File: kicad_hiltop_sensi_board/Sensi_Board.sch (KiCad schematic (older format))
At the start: 146 parts, among them J1 Conn_02x06_Counter_Clockwise, J10 Conn_ARM_JTAG_SWD_10, J2 Conn_02x06_Counter_Clockwise, J3 Conn_03x32_DIN41612, J4 Conn_02x06_Counter_Clockwise, J5 Conn_02x06_Counter_Clockwise, J6 Conn_02x06_Counter_Clockwise, J7 Conn_02x06_Counter_Clockwise, J8 Conn_02x06_Counter_Clockwise, U1 INA250A4, U2 LD1117S33TR_SOT223, U3 AT25DN512CSSHF-B, U6 LM75B

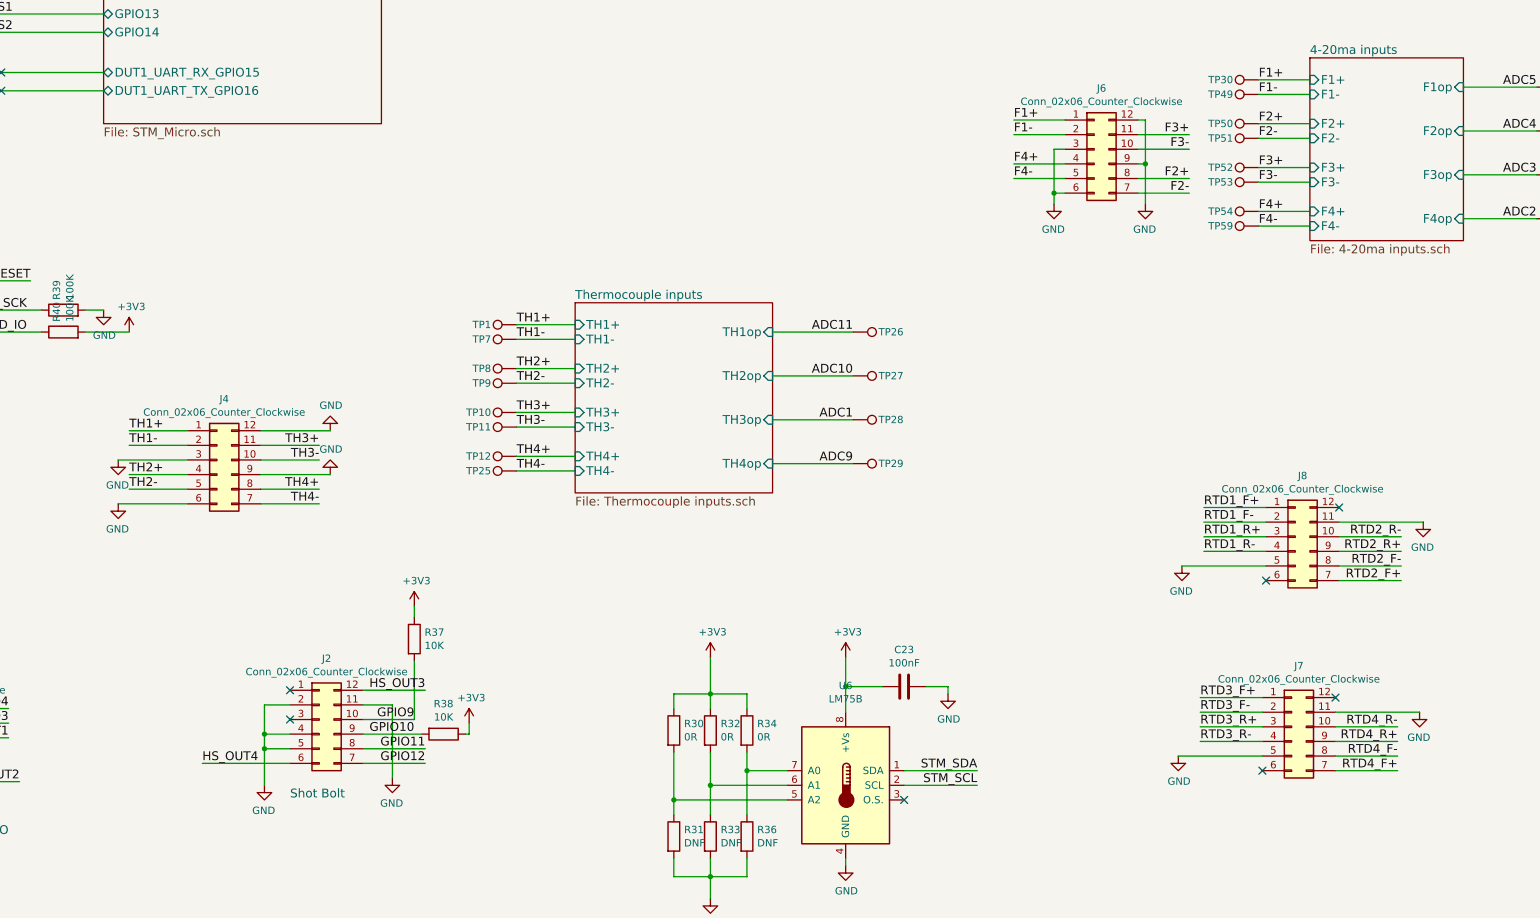
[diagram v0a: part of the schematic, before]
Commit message: Most of the routing of the sensi board complete
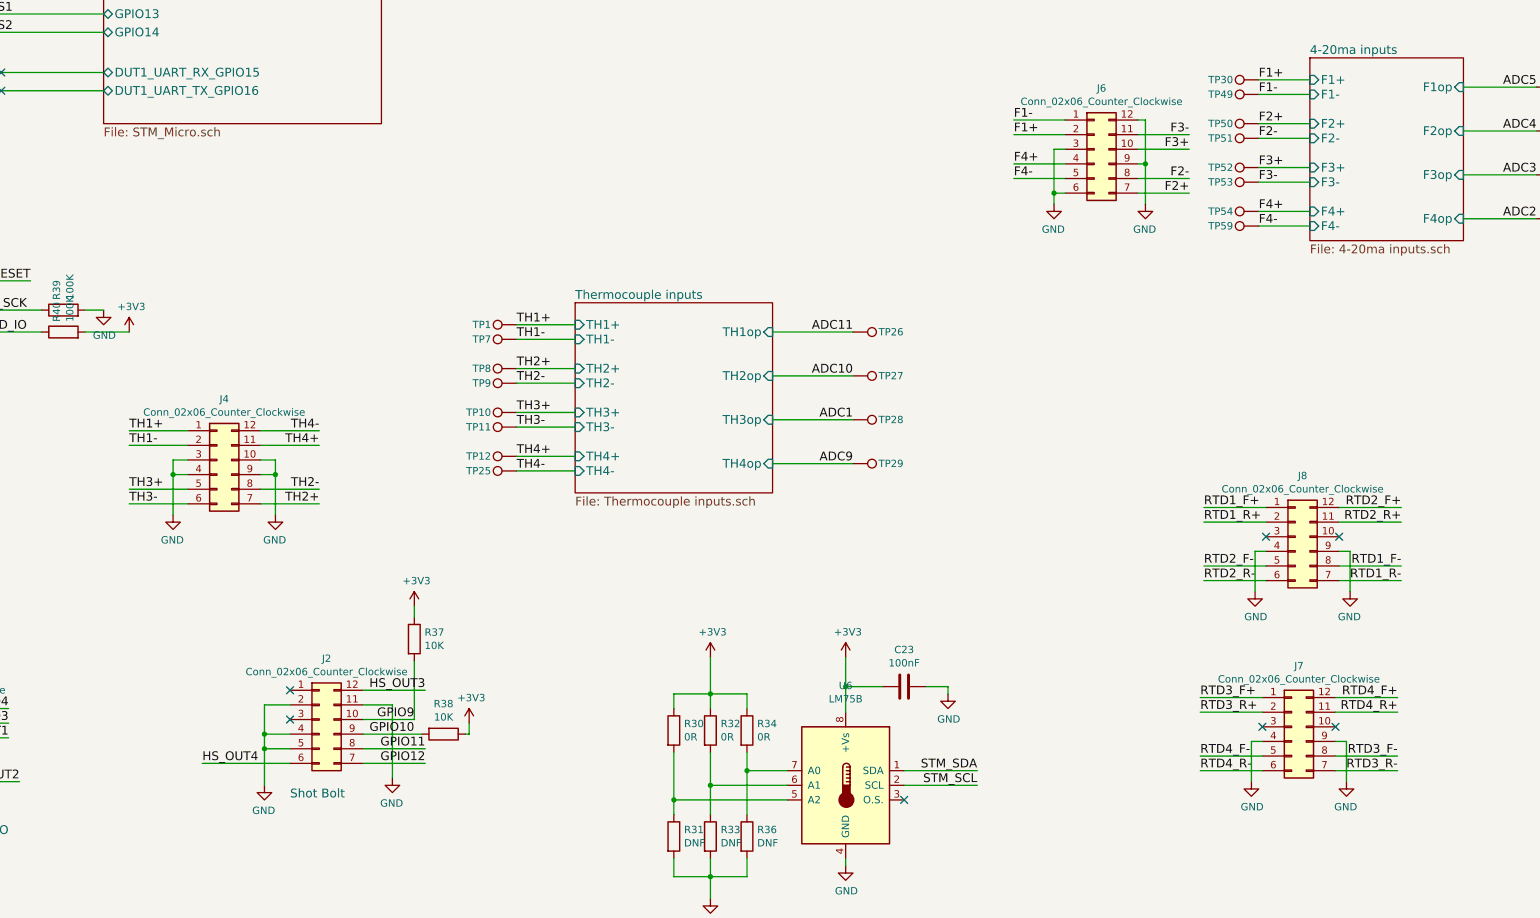
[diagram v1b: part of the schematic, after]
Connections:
- wire segments 522 -> 530
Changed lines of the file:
@@
 RTD3_R-
 Wire Wire Line
-	11150 11150 10725 11150
-Wire Wire Line
-	10725 11050 11150 11050
-Wire Wire Line
-	11150 11250 10725 11250
-Text Label 10725 11050 0    60   ~ 0
-RTD3_F+
-Text Label 10725 11150 0    60   ~ 0
-RTD3_F-
-Text Label 10725 11250 0    60   ~ 0
-RTD3_R+
-Text Label 10725 11350 0    60   ~ 0
-RTD3_R-
+	11650 11050 12075 11050
 Wire Wire Line
 	14475 12075 14050 12075
@@
 	14475 11550 14050 11550
 Wire Wire Line
-	11150 11350 10725 11350
+	11650 11150 12075 11150
 Text Label 6050 8500 0    60   ~ 0
 TH1+
@@
 TH1-
 Wire Wire Line
-	3800 9525 3400 9525
+	4300 9225 4700 9225
+Wire Wire Line
+	4300 9325 4700 9325
+Text Label 4700 9725 2    60   ~ 0
+TH2+
+Text Label 4700 9625 2    60   ~ 0
+TH2-
 Wire Wire Line
 	3800 9625 3400 9625
-Text Label 3400 9525 0    60   ~ 0
-TH2+
+Wire Wire Line
+	3800 9725 3400 9725
 Text Label 3400 9625 0    60   ~ 0
-TH2-
-Wire Wire Line
-	4300 9325 4700 9325
-Wire Wire Line
-	4300 9425 4700 9425
+TH3+
+Text Label 3400 9725 0    60   ~ 0
+TH3-
+Wire Wire Line
+	4300 9625 4700 9625
+Wire Wire Line
+	4300 9725 4700 9725
 Text Label 4700 9325 2    60   ~ 0
-TH3+
-Text Label 4700 9425 2    60   ~ 0
-TH3-
-Wire Wire Line
-	4300 9625 4700 9625
-Wire Wire Line
-	4300 9725 4700 9725
-Text Label 4700 9625 2    60   ~ 0
 TH4+
-Text Label 4700 9725 2    60   ~ 0
+Text Label 4700 9225 2    60   ~ 0
 TH4-
 Wire Wire Line
@@
 L power:GND #PWR0106
 U 1 1 5E8A9D77
-P 3325 9425
-F 0 "#PWR0106" H 3325 9175 50  0001 C CNN
-F 1 "GND" H 3330 9252 50  0000 C CNN
-F 2 "" H 3325 9425 50  0001 C CNN
-F 3 "" H 3325 9425 50  0001 C CNN
-	1    3325 9425
+P 3700 9800
+F 0 "#PWR0106" H 3700 9550 50  0001 C CNN
+F 1 "GND" H 3705 9627 50  0000 C CNN
+F 2 "" H 3700 9800 50  0001 C CNN
+F 3 "" H 3700 9800 50  0001 C CNN
+	1    3700 9800
 	-1   0    0    -1
 $EndComp
-Wire Wire Line
-	3800 9425 3325 9425
 $Comp
 L power:GND #PWR0107
 U 1 1 5E9010FA
-P 3325 9725
-F 0 "#PWR0107" H 3325 9475 50  0001 C CNN
-F 1 "GND" H 3330 9552 50  0000 C CNN
-F 2 "" H 3325 9725 50  0001 C CNN
-F 3 "" H 3325 9725 50  0001 C CNN
-	1    3325 9725
+P 4400 9800
+F 0 "#PWR0107" H 4400 9550 50  0001 C CNN
+F 1 "GND" H 4405 9627 50  0000 C CNN
+F 2 "" H 4400 9800 50  0001 C CNN
+F 3 "" H 4400 9800 50  0001 C CNN
+	1    4400 9800
 	-1   0    0    -1
 $EndComp
-Wire Wire Line
-	3800 9725 3325 9725
-$Comp
-L power:GND #PWR0108
-U 1 1 5E9587C9
-P 4775 9525
-F 0 "#PWR0108" H 4775 9275 50  0001 C CNN
-F 1 "GND" H 4780 9352 50  0000 C CNN
-F 2 "" H 4775 9525 50  0001 C CNN
-F 3 "" H 4775 9525 50  0001 C CNN
-	1    4775 9525
-	1    0    0    1
-$EndComp
-Wire Wire Line
-	4300 9525 4775 9525
-$Comp
-L power:GND #PWR0198
-U 1 1 5E9B0679
-P 4775 9225
-F 0 "#PWR0198" H 4775 8975 50  0001 C CNN
-F 1 "GND" H 4780 9052 50  0000 C CNN
-F 2 "" H 4775 9225 50  0001 C CNN
-F 3 "" H 4775 9225 50  0001 C CNN
-	1    4775 9225
-	1    0    0    1
-$EndComp
-Wire Wire Line
-	4300 9225 4775 9225
 Text Label 2575 11325 2    60   ~ 0
 HS_OUT1
@@
 Wire Wire Line
 	9800 7200 9450 7200
+Text Label 9450 7100 0    60   ~ 0
+F1-
 Text Label 9450 7200 0    60   ~ 0
-F1-
-Text Label 9450 7100 0    60   ~ 0
 F1+
 Wire Wire Line
@@
 Wire Wire Line
 	10300 7300 10650 7300
+Text Label 10650 7300 2    60   ~ 0
+F3+
 Text Label 10650 7200 2    60   ~ 0
-F3+
-Text Label 10650 7300 2    60   ~ 0
 F3-
 Wire Wire Line
@@
 $EndComp
 Wire Wire Line
+	11675 10150 12100 10150
+Wire Wire Line
+	10750 9750 11175 9750
+Wire Wire Line
 	11175 9850 10750 9850
 Wire Wire Line
-	10750 9750 11175 9750
-Wire Wire Line
-	11175 9950 10750 9950
-Wire Wire Line
-	11175 10050 10750 10050
+	11675 10250 12100 10250
 Text Label 10750 9750 0    60   ~ 0
 RTD1_F+
+Text Label 12100 10150 2    60   ~ 0
+RTD1_F-
 Text Label 10750 9850 0    60   ~ 0
-RTD1_F-
-Text Label 10750 9950 0    60   ~ 0
 RTD1_R+
-Text Label 10750 10050 0    60   ~ 0
+Text Label 12100 10250 2    60   ~ 0
 RTD1_R-
 Wire Wire Line
-	11175 10150 10600 10150
-$Comp
-L power:GND #PWR0258
-U 1 1 5D917155
-P 10600 10150
-F 0 "#PWR0258" H 10600 9900 50  0001 C CNN
-F 1 "GND" H 10605 9977 50  0000 C CNN
-F 2 "" H 10600 10150 50  0001 C CNN
-F 3 "" H 10600 10150 50  0001 C CNN
-	1    10600 10150
-	-1   0    0    -1
-$EndComp
-Wire Wire Line
-	11675 10150 12100 10150
-Wire Wire Line
-	12100 10250 11675 10250
-Wire Wire Line
-	11675 10050 12100 10050
-Wire Wire Line
-	11675 9950 12100 9950
-Text Label 12100 10250 2    60   ~ 0
+	11175 10150 10750 10150
+Wire Wire Line
+	12100 9750 11675 9750
+Wire Wire Line
+	11675 9850 12100 9850
+Wire Wire Line
+	11175 10250 10750 10250
+Text Label 12100 9750 2    60   ~ 0
 RTD2_F+
-Text Label 12100 10150 2    60   ~ 0
+Text Label 10750 10150 0    60   ~ 0
 RTD2_F-
-Text Label 12100 10050 2    60   ~ 0
+Text Label 12100 9850 2    60   ~ 0
 RTD2_R+
-Text Label 12100 9950 2    60   ~ 0
-RTD2_R-
-$Comp
-L power:GND #PWR0261
-U 1 1 5D9F6FB6
-P 12250 9850
-F 0 "#PWR0261" H 12250 9600 50  0001 C CNN
-F 1 "GND" H 12255 9677 50  0000 C CNN
-F 2 "" H 12250 9850 50  0001 C CNN
-F 3 "" H 12250 9850 50  0001 C CNN
-	1    12250 9850
-	-1   0    0    -1
-$EndComp
-Wire Wire Line
-	11675 9850 12250 9850
 $Comp
 L power:GND #PWR0262
 U 1 1 5DCE6CB8
-P 10575 11450
-F 0 "#PWR0262" H 10575 11200 50  0001 C CNN
-F 1 "GND" H 10580 11277 50  0000 C CNN
-F 2 "" H 10575 11450 50  0001 C CNN
-F 3 "" H 10575 11450 50  0001 C CNN
-	1    10575 11450
-	1    0    0    -1
-$EndComp
-Wire Wire Line
-	11150 11450 10575 11450
+P 11075 11625
+F 0 "#PWR0262" H 11075 11375 50  0001 C CNN
+F 1 "GND" H 11080 11452 50  0000 C CNN
+F 2 "" H 11075 11625 50  0001 C CNN
+F 3 "" H 11075 11625 50  0001 C CNN
+	1    11075 11625
+	1    0    0    -1
+$EndComp
 Wire Wire Line
 	11650 11450 12075 11450
 Wire Wire Line
-	12075 11550 11650 11550
-Wire Wire Line
-	11650 11350 12075 11350
-Wire Wire Line
-	11650 11250 12075 11250
-Text Label 12075 11550 2    60   ~ 0
-RTD4_F+
-Text Label 12075 11450 2    60   ~ 0
+	10725 11450 11150 11450
+Wire Wire Line
+	11150 11550 10725 11550
+Wire Wire Line
+	11650 11550 12075 11550
+Text Label 10725 11450 0    60   ~ 0
 RTD4_F-
-Text Label 12075 11350 2    60   ~ 0
-RTD4_R+
-Text Label 12075 11250 2    60   ~ 0
-RTD4_R-
 $Comp
 L power:GND #PWR0263
 U 1 1 5DDB9CAA
-P 12225 11150
-F 0 "#PWR0263" H 12225 10900 50  0001 C CNN
-F 1 "GND" H 12230 10977 50  0000 C CNN
-F 2 "" H 12225 11150 50  0001 C CNN
-F 3 "" H 12225 11150 50  0001 C CNN
-	1    12225 11150
+P 11725 11625
+F 0 "#PWR0263" H 11725 11375 50  0001 C CNN
+F 1 "GND" H 11730 11452 50  0000 C CNN
+F 2 "" H 11725 11625 50  0001 C CNN
+F 3 "" H 11725 11625 50  0001 C CNN
+	1    11725 11625
 	-1   0    0    -1
 $EndComp
-Wire Wire Line
-	11650 11150 12225 11150
-NoConn ~ 11175 10250
-NoConn ~ 11675 9750
-NoConn ~ 11150 11550
-NoConn ~ 11650 11050
 $Comp
 L Connector:Conn_02x06_Counter_Clockwise J8
@@
 	1    0    0    -1
 $EndComp
+Text Label 10650 7500 2    60   ~ 0
+F2-
 Text Label 10650 7600 2    60   ~ 0
-F2-
-Text Label 10650 7500 2    60   ~ 0
 F2+
 Wire Wire Line
@@
 	0    -1   -1   0
 $EndComp
+Wire Wire Line
+	3800 9525 3700 9525
+Wire Wire Line
+	3800 9425 3700 9425
+Wire Wire Line
+	3700 9425 3700 9525
+Connection ~ 3700 9525
+Wire Wire Line
+	3700 9525 3700 9800
+Wire Wire Line
+	4300 9425 4400 9425
+Wire Wire Line
+	4400 9425 4400 9525
+Wire Wire Line
+	4300 9525 4400 9525
+Connection ~ 4400 9525
+Wire Wire Line
+	4400 9525 4400 9800
+NoConn ~ 11150 11250
+NoConn ~ 11650 11250
+Wire Wire Line
+	11075 11625 11075 11350
+Wire Wire Line
+	11075 11350 11150 11350
+Wire Wire Line
+	11650 11350 11725 11350
+Wire Wire Line
+	11725 11350 11725 11625
+Text Label 10725 11150 0    60   ~ 0
+RTD3_R+
+Text Label 10725 11050 0    60   ~ 0
+RTD3_F+
+Wire Wire Line
+	10725 11150 11150 11150
+Wire Wire Line
+	11150 11050 10725 11050
+Text Label 10725 11550 0    60   ~ 0
+RTD4_R-
+Text Label 12075 11450 2    60   ~ 0
+RTD3_F-
+Text Label 12075 11050 2    60   ~ 0
+RTD4_F+
+Text Label 12075 11150 2    60   ~ 0
+RTD4_R+
+Text Label 12075 11550 2    60   ~ 0
+RTD3_R-
+$Comp
+L power:GND #PWR0108
+U 1 1 5EE7D394
+P 11100 10325
+F 0 "#PWR0108" H 11100 10075 50  0001 C CNN
+F 1 "GND" H 11105 10152 50  0000 C CNN
+F 2 "" H 11100 10325 50  0001 C CNN
+F 3 "" H 11100 10325 50  0001 C CNN
+	1    11100 10325
+	1    0    0    -1
+$EndComp
+$Comp
+L power:GND #PWR0147
+U 1 1 5EE7D39F
+P 11750 10325
+F 0 "#PWR0147" H 11750 10075 50  0001 C CNN
+F 1 "GND" H 11755 10152 50  0000 C CNN
+F 2 "" H 11750 10325 50  0001 C CNN
+F 3 "" H 11750 10325 50  0001 C CNN
+	1    11750 10325
+	-1   0    0    -1
+$EndComp
+NoConn ~ 11175 9950
+NoConn ~ 11675 9950
+Wire Wire Line
+	11100 10325 11100 10050
+Wire Wire Line
+	11100 10050 11175 10050
+Wire Wire Line
+	11675 10050 11750 10050
+Wire Wire Line
+	11750 10050 11750 10325
+Text Label 10750 10250 0    60   ~ 0
+RTD2_R-
 $EndSCHEMATC
